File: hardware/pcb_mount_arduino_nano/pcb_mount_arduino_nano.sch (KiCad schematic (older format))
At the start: 1 part

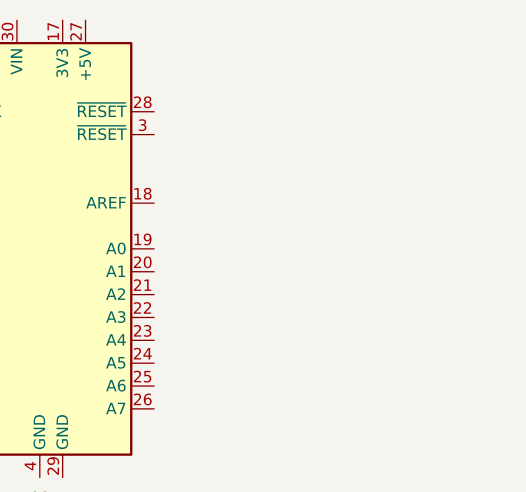
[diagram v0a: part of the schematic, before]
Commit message: Add mounting holes and DS18B20
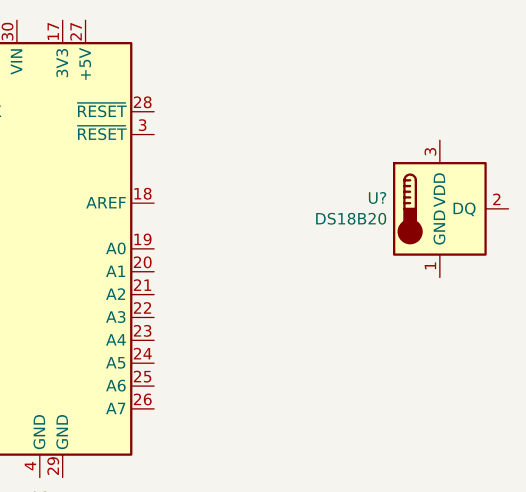
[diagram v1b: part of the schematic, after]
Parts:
- added U?: DS18B20, Package_TO_SOT_THT:TO-92_Inline, symbol Sensor_Temperature:DS18B20
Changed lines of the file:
@@
+	1    0    0    -1
+$EndComp
+$Comp
+L Sensor_Temperature:DS18B20 U?
+U 1 1 5F57B029
+P 5750 2350
+F 0 "U?" H 5520 2396 50  0000 R CNN
+F 1 "DS18B20" H 5520 2305 50  0000 R CNN
+F 2 "Package_TO_SOT_THT:TO-92_Inline" H 4750 2100 50  0001 C CNN
+F 3 "http://datasheets.maximintegrated.com/en/ds/DS18B20.pdf" H 5600 2600 50  0001 C CNN
+	1    5750 2350
 	1    0    0    -1
 $EndComp

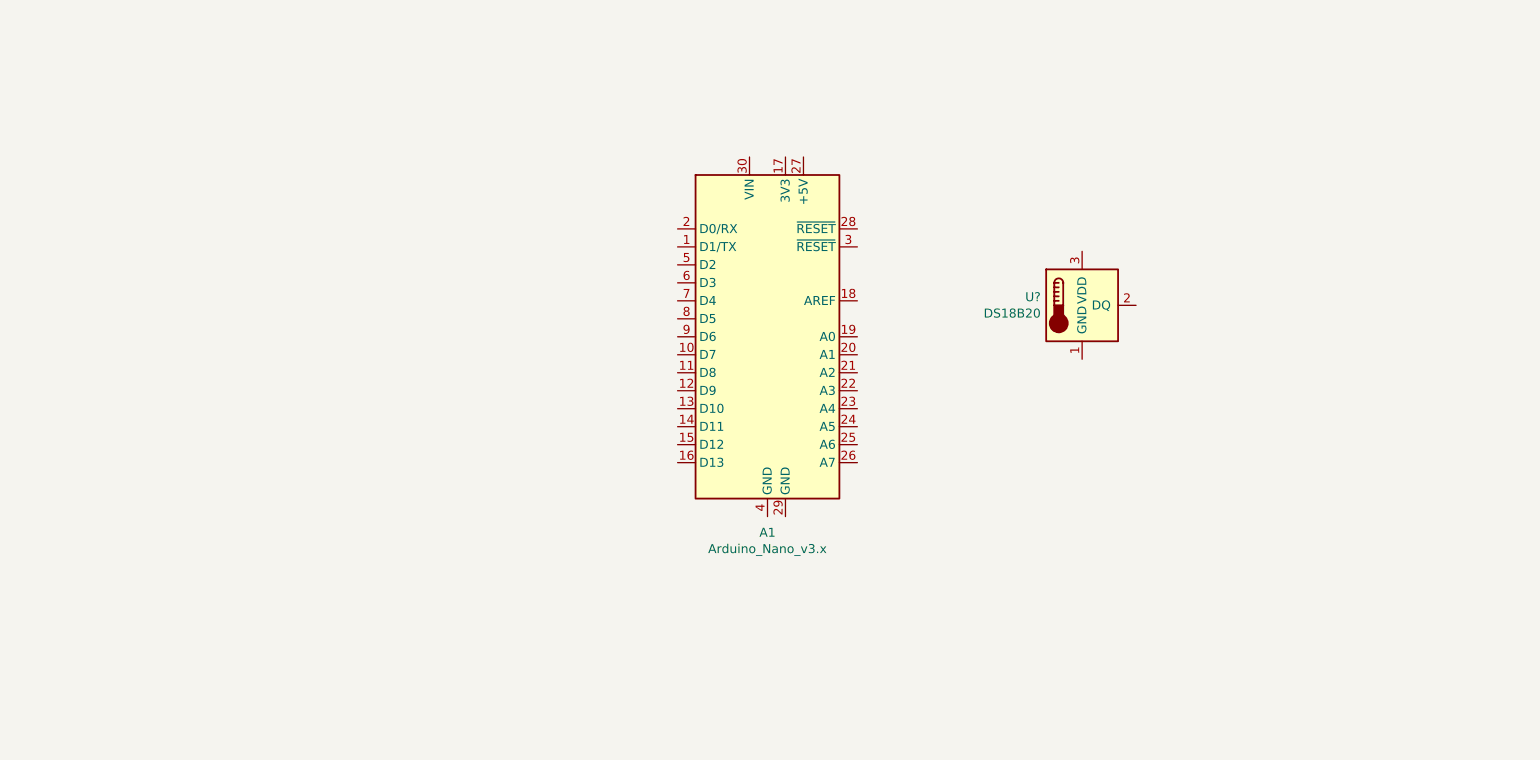
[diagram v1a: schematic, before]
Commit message: Add serial port and power connector
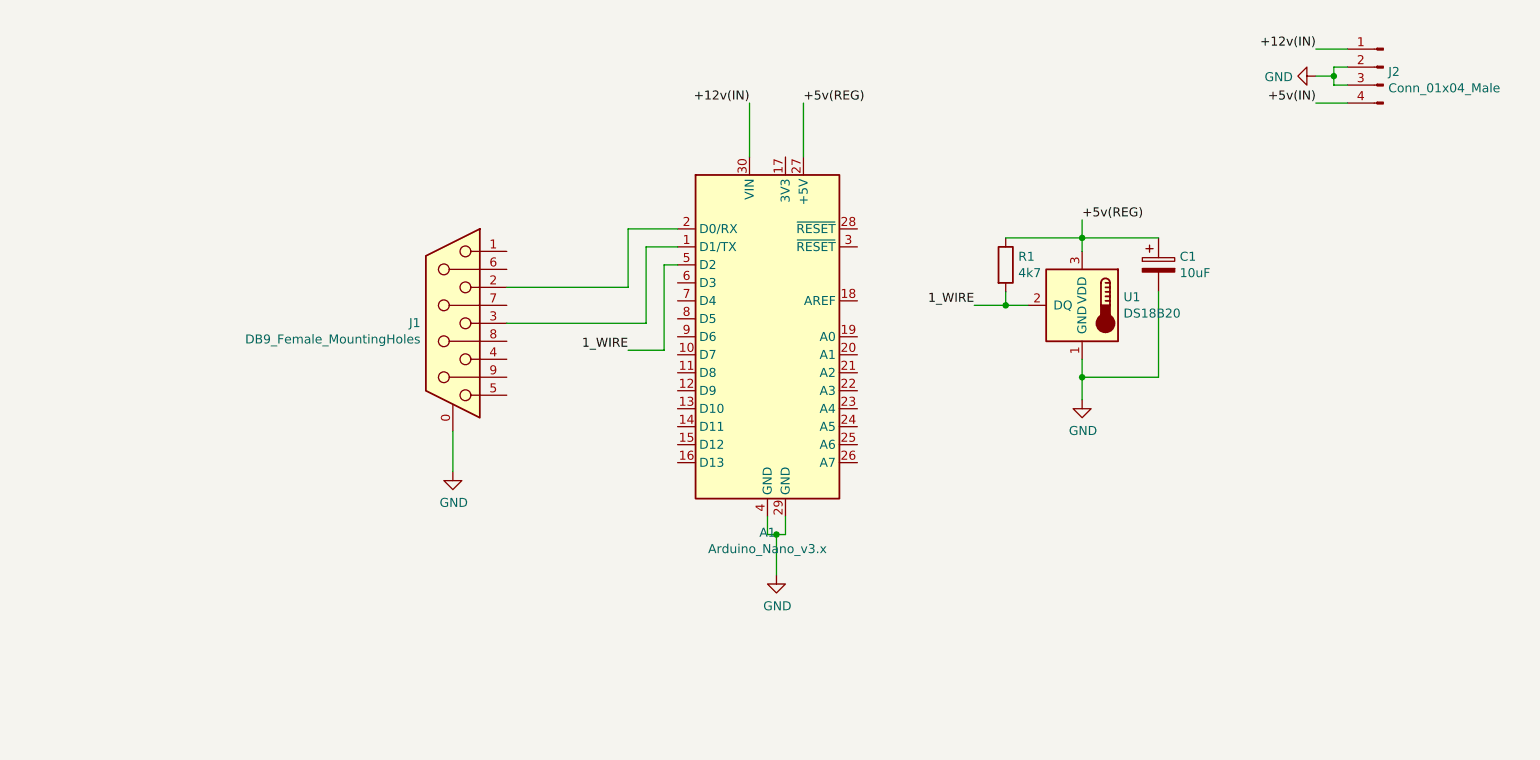
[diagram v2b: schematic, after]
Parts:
- added C1: 10uF, Capacitor_THT:CP_Radial_D5.0mm_P2.00mm, symbol Device:CP
- added J1: DB9_Female_MountingHoles, Connector_Dsub:DSUB-9_Female_Vertical_P2.77x2.84mm_MountingHoles, symbol Connector:DB9_Female_MountingHoles
- added J2: Conn_01x04_Male, Connector_TE-Connectivity:TE_MATE-N-LOK_350211-1_1x04_P5.08mm_Vertical, symbol Connector:Conn_01x04_Male
- added R1: 4k7, Resistor_THT:R_Axial_DIN0207_L6.3mm_D2.5mm_P10.16mm_Horizontal, symbol Device:R
- gave numbers to parts that had none: 1
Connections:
- net at A1.1 (D1/TX): now also J1.3
- net at A1.2 (D0/RX): now also J1.2
- net +5v(REG): now reaches A1.27 (+5V)
- net +5v(REG): now also U1.3 (VDD), C1.1, R1.1
- net GND: now reaches A1.29 (GND)
- net GND: now also A1.4 (GND), U1.1 (GND), C1.2, J1.0 (PAD), J2.2 (Pin_2), J2.3 (Pin_3)
- net +12v(IN): now reaches A1.30 (VIN)
- net +12v(IN): now also J2.1 (Pin_1)
- net 1_WIRE: now reaches A1.5 (D2)
- net 1_WIRE: now also U1.2 (DQ), R1.2
- new net +5v(IN): J2.4 (Pin_4)
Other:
- moved on the sheet: U1
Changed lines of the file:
@@
 $EndComp
 $Comp
-L Sensor_Temperature:DS18B20 U?
+L Sensor_Temperature:DS18B20 U1
 U 1 1 5F57B029
 P 5750 2350
-F 0 "U?" H 5520 2396 50  0000 R CNN
+F 0 "U1" H 5520 2396 50  0000 R CNN
 F 1 "DS18B20" H 5520 2305 50  0000 R CNN
 F 2 "Package_TO_SOT_THT:TO-92_Inline" H 4750 2100 50  0001 C CNN
 F 3 "http://datasheets.maximintegrated.com/en/ds/DS18B20.pdf" H 5600 2600 50  0001 C CNN
 	1    5750 2350
+	-1   0    0    -1
+$EndComp
+Text Label 4200 1225 0    50   ~ 0
++5v(REG)
+Text Label 5750 1875 0    50   ~ 0
++5v(REG)
+Wire Wire Line
+	5750 2050 5750 1975
+Wire Wire Line
+	4200 1225 4200 1525
+$Comp
+L power:GND #PWR0101
+U 1 1 5F57CAD8
+P 5750 2875
+F 0 "#PWR0101" H 5750 2625 50  0001 C CNN
+F 1 "GND" H 5755 2702 50  0000 C CNN
+F 2 "" H 5750 2875 50  0001 C CNN
+F 3 "" H 5750 2875 50  0001 C CNN
+	1    5750 2875
 	1    0    0    -1
 $EndComp
+$Comp
+L power:GND #PWR0102
+U 1 1 5F57DBDC
+P 4050 3850
+F 0 "#PWR0102" H 4050 3600 50  0001 C CNN
+F 1 "GND" H 4055 3677 50  0000 C CNN
+F 2 "" H 4050 3850 50  0001 C CNN
+F 3 "" H 4050 3850 50  0001 C CNN
+	1    4050 3850
+	1    0    0    -1
+$EndComp
+Wire Wire Line
+	5750 2650 5750 2750
+Wire Wire Line
+	4100 3525 4100 3625
+Wire Wire Line
+	4100 3625 4050 3625
+Wire Wire Line
+	4050 3625 4050 3850
+Wire Wire Line
+	4000 3525 4000 3625
+Wire Wire Line
+	4000 3625 4050 3625
+Connection ~ 4050 3625
+$Comp
+L power:GND #PWR0103
+U 1 1 5F57FD3D
+P 2250 3275
+F 0 "#PWR0103" H 2250 3025 50  0001 C CNN
+F 1 "GND" H 2255 3102 50  0000 C CNN
+F 2 "" H 2250 3275 50  0001 C CNN
+F 3 "" H 2250 3275 50  0001 C CNN
+	1    2250 3275
+	1    0    0    -1
+$EndComp
+Wire Wire Line
+	2250 3050 2250 3275
+$Comp
+L Connector:DB9_Female_MountingHoles J1
+U 1 1 5F57E806
+P 2250 2450
+F 0 "J1" H 2430 2452 50  0000 L CNN
+F 1 "DB9_Female_MountingHoles" H 2430 2361 50  0000 L CNN
+F 2 "Connector_Dsub:DSUB-9_Female_Vertical_P2.77x2.84mm_MountingHoles" H 2250 2450 50  0001 C CNN
+F 3 " ~" H 2250 2450 50  0001 C CNN
+	1    2250 2450
+	-1   0    0    -1
+$EndComp
+Wire Wire Line
+	2550 2250 3225 2250
+Wire Wire Line
+	3225 2250 3225 1925
+Wire Wire Line
+	3225 1925 3500 1925
+Wire Wire Line
+	3500 2025 3325 2025
+Wire Wire Line
+	3325 2025 3325 2450
+Wire Wire Line
+	3325 2450 2550 2450
+Text Label 5150 2350 2    50   ~ 0
+1_WIRE
+Wire Wire Line
+	5150 2350 5325 2350
+Text Label 3225 2600 2    50   ~ 0
+1_WIRE
+Wire Wire Line
+	3500 2125 3425 2125
+Wire Wire Line
+	3425 2125 3425 2600
+Wire Wire Line
+	3425 2600 3225 2600
+$Comp
+L Device:R R1
+U 1 1 5F583C5E
+P 5325 2125
+F 0 "R1" H 5395 2171 50  0000 L CNN
+F 1 "4k7" H 5395 2080 50  0000 L CNN
+F 2 "Resistor_THT:R_Axial_DIN0207_L6.3mm_D2.5mm_P10.16mm_Horizontal" V 5255 2125 50  0001 C CNN
+F 3 "~" H 5325 2125 50  0001 C CNN
+	1    5325 2125
+	1    0    0    -1
+$EndComp
+Wire Wire Line
+	5325 1975 5750 1975
+Connection ~ 5750 1975
+Wire Wire Line
+	5750 1975 5750 1875
+Wire Wire Line
+	5325 2275 5325 2350
+Connection ~ 5325 2350
+Wire Wire Line
+	5325 2350 5450 2350
+$Comp
+L Device:CP C1
+U 1 1 5F584A00
+P 6175 2125
+F 0 "C1" H 6293 2171 50  0000 L CNN
+F 1 "10uF" H 6293 2080 50  0000 L CNN
+F 2 "Capacitor_THT:CP_Radial_D5.0mm_P2.00mm" H 6213 1975 50  0001 C CNN
+F 3 "~" H 6175 2125 50  0001 C CNN
+	1    6175 2125
+	1    0    0    -1
+$EndComp
+Wire Wire Line
+	5750 1975 6175 1975
+Wire Wire Line
+	6175 2275 6175 2750
+Wire Wire Line
+	6175 2750 5750 2750
+Connection ~ 5750 2750
+Wire Wire Line
+	5750 2750 5750 2875
+Text Label 7050 925  2    50   ~ 0
++12v(IN)
+Text Label 7050 1225 2    50   ~ 0
++5v(IN)
+$Comp
+L power:GND #PWR0104
+U 1 1 5F58916E
+P 7050 1075
+F 0 "#PWR0104" H 7050 825 50  0001 C CNN
+F 1 "GND" V 7055 947 50  0000 R CNN
+F 2 "" H 7050 1075 50  0001 C CNN
+F 3 "" H 7050 1075 50  0001 C CNN
+	1    7050 1075
+	0    1    1    0
+$EndComp
+Wire Wire Line
+	7150 1125 7150 1075
+Wire Wire Line
+	7150 1075 7050 1075
+Wire Wire Line
+	7150 1025 7150 1075
+Connection ~ 7150 1075
+Wire Wire Line
+	7225 1125 7150 1125
+Wire Wire Line
+	7225 1025 7150 1025
+$Comp
+L Connector:Conn_01x04_Male J2
+U 1 1 5F58C7FF
+P 7425 1025
+F 0 "J2" H 7397 999 50  0000 R CNN
+F 1 "Conn_01x04_Male" H 7397 908 50  0000 R CNN
+F 2 "Connector_TE-Connectivity:TE_MATE-N-LOK_350211-1_1x04_P5.08mm_Vertical" H 7425 1025 50  0001 C CNN
+F 3 "~" H 7425 1025 50  0001 C CNN
+	1    7425 1025
+	-1   0    0    -1
+$EndComp
+Wire Wire Line
+	7050 1225 7225 1225
+Wire Wire Line
+	7050 925  7225 925
+Text Label 3900 1225 2    50   ~ 0
++12v(IN)
+Wire Wire Line
+	3900 1525 3900 1225
 $EndSCHEMATC

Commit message: Add multiple 1 wire temperature sensors
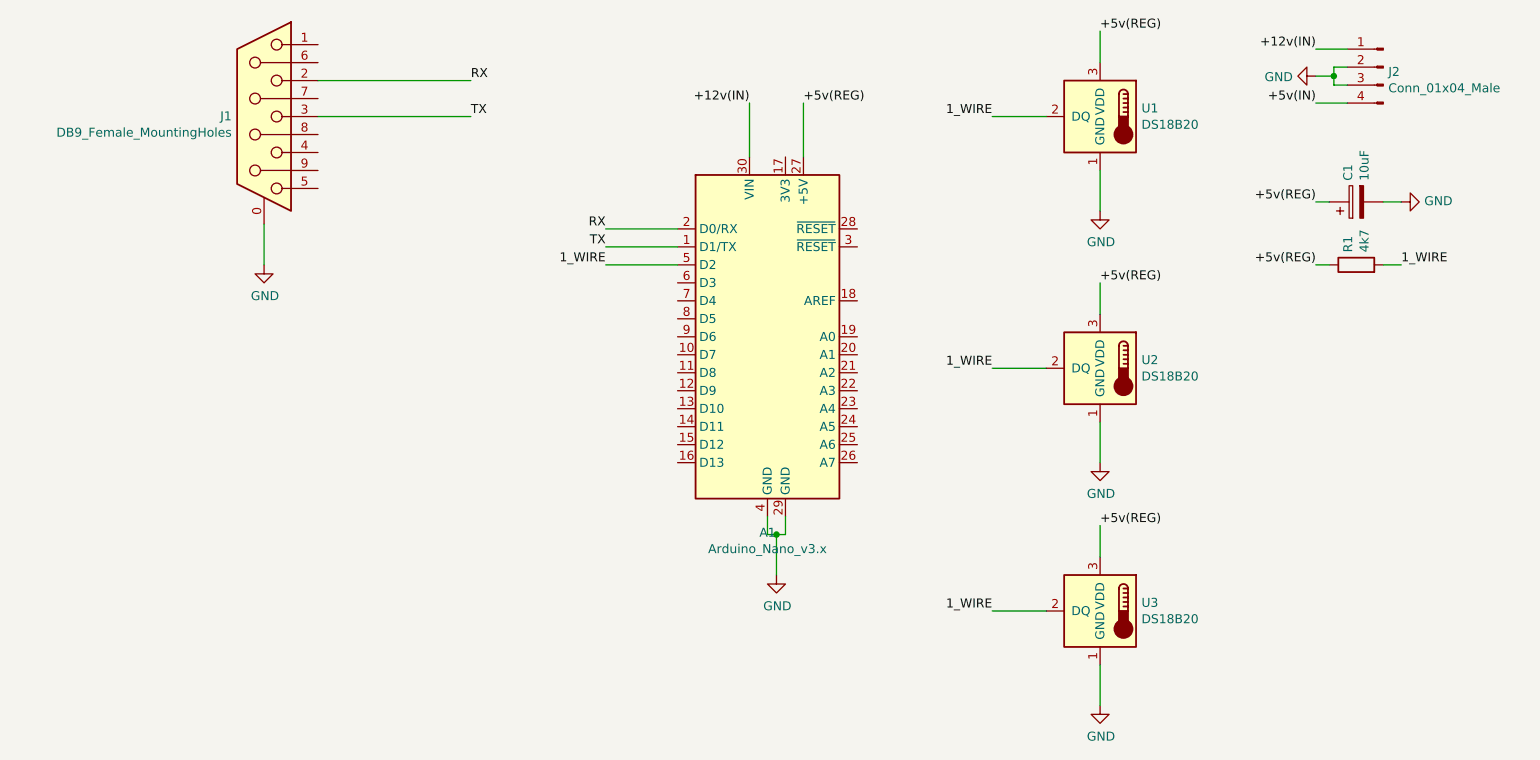
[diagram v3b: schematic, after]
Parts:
- added U2, U3: DS18B20, Package_TO_SOT_THT:TO-92_Inline, symbol Sensor_Temperature:DS18B20
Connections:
- net +5v(REG): now also U2.3 (VDD), U3.3 (VDD)
- net 1_WIRE: now also U2.2 (DQ), U3.2 (DQ)
- net GND: now also U2.1 (GND), U3.1 (GND)
- net TX: now reaches A1.1 (D1/TX), J1.3
- net RX: now reaches A1.2 (D0/RX), J1.2
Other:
- moved on the sheet: C1, J1, R1, U1
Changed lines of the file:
@@
 L Sensor_Temperature:DS18B20 U1
 U 1 1 5F57B029
-P 5750 2350
-F 0 "U1" H 5520 2396 50  0000 R CNN
-F 1 "DS18B20" H 5520 2305 50  0000 R CNN
-F 2 "Package_TO_SOT_THT:TO-92_Inline" H 4750 2100 50  0001 C CNN
-F 3 "http://datasheets.maximintegrated.com/en/ds/DS18B20.pdf" H 5600 2600 50  0001 C CNN
-	1    5750 2350
+P 5850 1300
+F 0 "U1" H 5620 1346 50  0000 R CNN
+F 1 "DS18B20" H 5620 1255 50  0000 R CNN
+F 2 "Package_TO_SOT_THT:TO-92_Inline" H 4850 1050 50  0001 C CNN
+F 3 "http://datasheets.maximintegrated.com/en/ds/DS18B20.pdf" H 5700 1550 50  0001 C CNN
+	1    5850 1300
 	-1   0    0    -1
 $EndComp
 Text Label 4200 1225 0    50   ~ 0
 +5v(REG)
-Text Label 5750 1875 0    50   ~ 0
-+5v(REG)
-Wire Wire Line
-	5750 2050 5750 1975
+Text Label 5850 825  0    50   ~ 0
++5v(REG)
 Wire Wire Line
 	4200 1225 4200 1525
@@
 L power:GND #PWR0101
 U 1 1 5F57CAD8
-P 5750 2875
-F 0 "#PWR0101" H 5750 2625 50  0001 C CNN
-F 1 "GND" H 5755 2702 50  0000 C CNN
-F 2 "" H 5750 2875 50  0001 C CNN
-F 3 "" H 5750 2875 50  0001 C CNN
-	1    5750 2875
+P 5850 1825
+F 0 "#PWR0101" H 5850 1575 50  0001 C CNN
+F 1 "GND" H 5855 1652 50  0000 C CNN
+F 2 "" H 5850 1825 50  0001 C CNN
+F 3 "" H 5850 1825 50  0001 C CNN
+	1    5850 1825
 	1    0    0    -1
 $EndComp
@@
 $EndComp
 Wire Wire Line
-	5750 2650 5750 2750
-Wire Wire Line
 	4100 3525 4100 3625
 Wire Wire Line
@@
 L power:GND #PWR0103
 U 1 1 5F57FD3D
-P 2250 3275
-F 0 "#PWR0103" H 2250 3025 50  0001 C CNN
-F 1 "GND" H 2255 3102 50  0000 C CNN
-F 2 "" H 2250 3275 50  0001 C CNN
-F 3 "" H 2250 3275 50  0001 C CNN
-	1    2250 3275
-	1    0    0    -1
-$EndComp
-Wire Wire Line
-	2250 3050 2250 3275
+P 1200 2125
+F 0 "#PWR0103" H 1200 1875 50  0001 C CNN
+F 1 "GND" H 1205 1952 50  0000 C CNN
+F 2 "" H 1200 2125 50  0001 C CNN
+F 3 "" H 1200 2125 50  0001 C CNN
+	1    1200 2125
+	1    0    0    -1
+$EndComp
+Wire Wire Line
+	1200 1900 1200 2125
 $Comp
 L Connector:DB9_Female_MountingHoles J1
 U 1 1 5F57E806
-P 2250 2450
-F 0 "J1" H 2430 2452 50  0000 L CNN
-F 1 "DB9_Female_MountingHoles" H 2430 2361 50  0000 L CNN
-F 2 "Connector_Dsub:DSUB-9_Female_Vertical_P2.77x2.84mm_MountingHoles" H 2250 2450 50  0001 C CNN
-F 3 " ~" H 2250 2450 50  0001 C CNN
-	1    2250 2450
-	-1   0    0    -1
-$EndComp
-Wire Wire Line
-	2550 2250 3225 2250
-Wire Wire Line
-	3225 2250 3225 1925
-Wire Wire Line
-	3225 1925 3500 1925
-Wire Wire Line
-	3500 2025 3325 2025
-Wire Wire Line
-	3325 2025 3325 2450
-Wire Wire Line
-	3325 2450 2550 2450
-Text Label 5150 2350 2    50   ~ 0
-1_WIRE
-Wire Wire Line
-	5150 2350 5325 2350
-Text Label 3225 2600 2    50   ~ 0
-1_WIRE
-Wire Wire Line
-	3500 2125 3425 2125
-Wire Wire Line
-	3425 2125 3425 2600
-Wire Wire Line
-	3425 2600 3225 2600
+P 1200 1300
+F 0 "J1" H 1380 1302 50  0000 L CNN
+F 1 "DB9_Female_MountingHoles" H 1380 1211 50  0000 L CNN
+F 2 "Connector_Dsub:DSUB-9_Female_Vertical_P2.77x2.84mm_MountingHoles" H 1200 1300 50  0001 C CNN
+F 3 " ~" H 1200 1300 50  0001 C CNN
+	1    1200 1300
+	-1   0    0    -1
+$EndComp
+Text Label 5250 1300 2    50   ~ 0
+1_WIRE
+Text Label 3100 2125 2    50   ~ 0
+1_WIRE
 $Comp
 L Device:R R1
 U 1 1 5F583C5E
-P 5325 2125
-F 0 "R1" H 5395 2171 50  0000 L CNN
-F 1 "4k7" H 5395 2080 50  0000 L CNN
-F 2 "Resistor_THT:R_Axial_DIN0207_L6.3mm_D2.5mm_P10.16mm_Horizontal" V 5255 2125 50  0001 C CNN
-F 3 "~" H 5325 2125 50  0001 C CNN
-	1    5325 2125
-	1    0    0    -1
-$EndComp
-Wire Wire Line
-	5325 1975 5750 1975
-Connection ~ 5750 1975
-Wire Wire Line
-	5750 1975 5750 1875
-Wire Wire Line
-	5325 2275 5325 2350
-Connection ~ 5325 2350
-Wire Wire Line
-	5325 2350 5450 2350
+P 7275 2125
+F 0 "R1" H 7345 2171 50  0000 L CNN
+F 1 "4k7" H 7345 2080 50  0000 L CNN
+F 2 "Resistor_THT:R_Axial_DIN0207_L6.3mm_D2.5mm_P10.16mm_Horizontal" V 7205 2125 50  0001 C CNN
+F 3 "~" H 7275 2125 50  0001 C CNN
+	1    7275 2125
+	0    -1   -1   0
+$EndComp
 $Comp
 L Device:CP C1
 U 1 1 5F584A00
-P 6175 2125
-F 0 "C1" H 6293 2171 50  0000 L CNN
-F 1 "10uF" H 6293 2080 50  0000 L CNN
-F 2 "Capacitor_THT:CP_Radial_D5.0mm_P2.00mm" H 6213 1975 50  0001 C CNN
-F 3 "~" H 6175 2125 50  0001 C CNN
-	1    6175 2125
-	1    0    0    -1
-$EndComp
-Wire Wire Line
-	5750 1975 6175 1975
-Wire Wire Line
-	6175 2275 6175 2750
-Wire Wire Line
-	6175 2750 5750 2750
-Connection ~ 5750 2750
-Wire Wire Line
-	5750 2750 5750 2875
+P 7275 1775
+F 0 "C1" H 7393 1821 50  0000 L CNN
+F 1 "10uF" H 7393 1730 50  0000 L CNN
+F 2 "Capacitor_THT:CP_Radial_D5.0mm_P2.00mm" H 7313 1625 50  0001 C CNN
+F 3 "~" H 7275 1775 50  0001 C CNN
+	1    7275 1775
+	0    -1   -1   0
+$EndComp
 Text Label 7050 925  2    50   ~ 0
 +12v(IN)
@@
 Wire Wire Line
 	3900 1525 3900 1225
+Text Label 7050 1775 2    50   ~ 0
++5v(REG)
+$Comp
+L power:GND #PWR0105
+U 1 1 5F5883E6
+P 7525 1775
+F 0 "#PWR0105" H 7525 1525 50  0001 C CNN
+F 1 "GND" V 7530 1647 50  0000 R CNN
+F 2 "" H 7525 1775 50  0001 C CNN
+F 3 "" H 7525 1775 50  0001 C CNN
+	1    7525 1775
+	0    -1   -1   0
+$EndComp
+Wire Wire Line
+	7425 1775 7525 1775
+Wire Wire Line
+	7050 1775 7125 1775
+Wire Wire Line
+	5850 1600 5850 1825
+Text Label 7525 2125 0    50   ~ 0
+1_WIRE
+Text Label 7050 2125 2    50   ~ 0
++5v(REG)
+Wire Wire Line
+	5850 825  5850 1000
+Wire Wire Line
+	5250 1300 5550 1300
+Wire Wire Line
+	7050 2125 7125 2125
+Wire Wire Line
+	7425 2125 7525 2125
+Text Label 2350 1100 0    50   ~ 0
+RX
+Text Label 2350 1300 0    50   ~ 0
+TX
+Text Label 3100 1925 2    50   ~ 0
+RX
+Text Label 3100 2025 2    50   ~ 0
+TX
+Wire Wire Line
+	1500 1100 2350 1100
+Wire Wire Line
+	1500 1300 2350 1300
+Wire Wire Line
+	3100 1925 3500 1925
+Wire Wire Line
+	3100 2025 3500 2025
+Wire Wire Line
+	3100 2125 3500 2125
+$Comp
+L Sensor_Temperature:DS18B20 U2
+U 1 1 5F599217
+P 5850 2700
+F 0 "U2" H 5620 2746 50  0000 R CNN
+F 1 "DS18B20" H 5620 2655 50  0000 R CNN
+F 2 "Package_TO_SOT_THT:TO-92_Inline" H 4850 2450 50  0001 C CNN
+F 3 "http://datasheets.maximintegrated.com/en/ds/DS18B20.pdf" H 5700 2950 50  0001 C CNN
+	1    5850 2700
+	-1   0    0    -1
+$EndComp
+Text Label 5850 2225 0    50   ~ 0
++5v(REG)
+$Comp
+L power:GND #PWR0106
+U 1 1 5F59921E
+P 5850 3225
+F 0 "#PWR0106" H 5850 2975 50  0001 C CNN
+F 1 "GND" H 5855 3052 50  0000 C CNN
+F 2 "" H 5850 3225 50  0001 C CNN
+F 3 "" H 5850 3225 50  0001 C CNN
+	1    5850 3225
+	1    0    0    -1
+$EndComp
+Text Label 5250 2700 2    50   ~ 0
+1_WIRE
+Wire Wire Line
+	5850 3000 5850 3225
+Wire Wire Line
+	5850 2225 5850 2400
+Wire Wire Line
+	5250 2700 5550 2700
+$Comp
+L Sensor_Temperature:DS18B20 U3
+U 1 1 5F59A5FC
+P 5850 4050
+F 0 "U3" H 5620 4096 50  0000 R CNN
+F 1 "DS18B20" H 5620 4005 50  0000 R CNN
+F 2 "Package_TO_SOT_THT:TO-92_Inline" H 4850 3800 50  0001 C CNN
+F 3 "http://datasheets.maximintegrated.com/en/ds/DS18B20.pdf" H 5700 4300 50  0001 C CNN
+	1    5850 4050
+	-1   0    0    -1
+$EndComp
+Text Label 5850 3575 0    50   ~ 0
++5v(REG)
+$Comp
+L power:GND #PWR0107
+U 1 1 5F59A603
+P 5850 4575
+F 0 "#PWR0107" H 5850 4325 50  0001 C CNN
+F 1 "GND" H 5855 4402 50  0000 C CNN
+F 2 "" H 5850 4575 50  0001 C CNN
+F 3 "" H 5850 4575 50  0001 C CNN
+	1    5850 4575
+	1    0    0    -1
+$EndComp
+Text Label 5250 4050 2    50   ~ 0
+1_WIRE
+Wire Wire Line
+	5850 4350 5850 4575
+Wire Wire Line
+	5850 3575 5850 3750
+Wire Wire Line
+	5250 4050 5550 4050
 $EndSCHEMATC
